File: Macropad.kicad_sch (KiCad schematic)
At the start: 19 parts, among them U1 Arduino_Pro_Micro

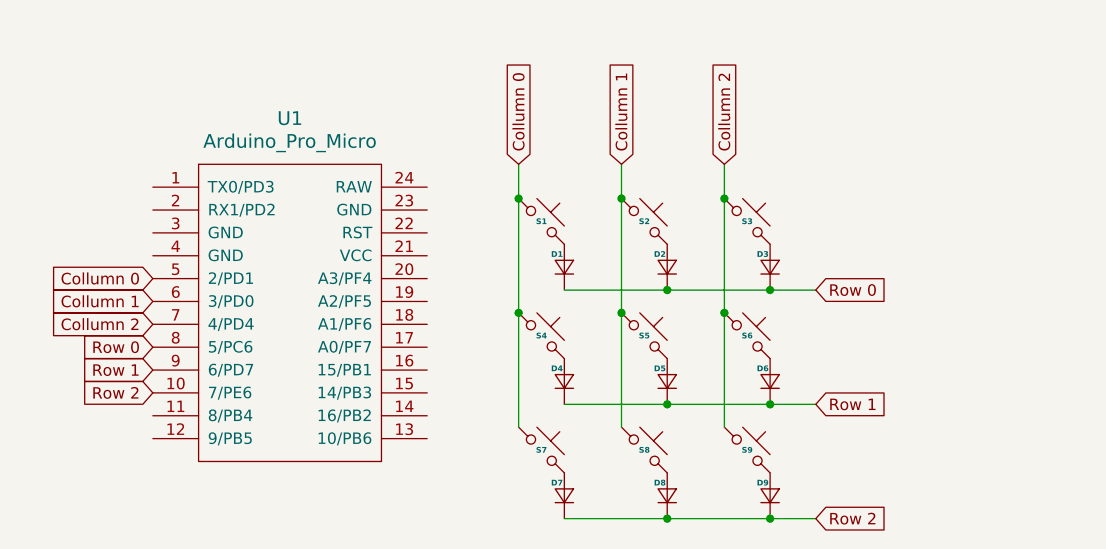
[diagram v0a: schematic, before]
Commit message: Change PCB dimension + add GND and Reset Button
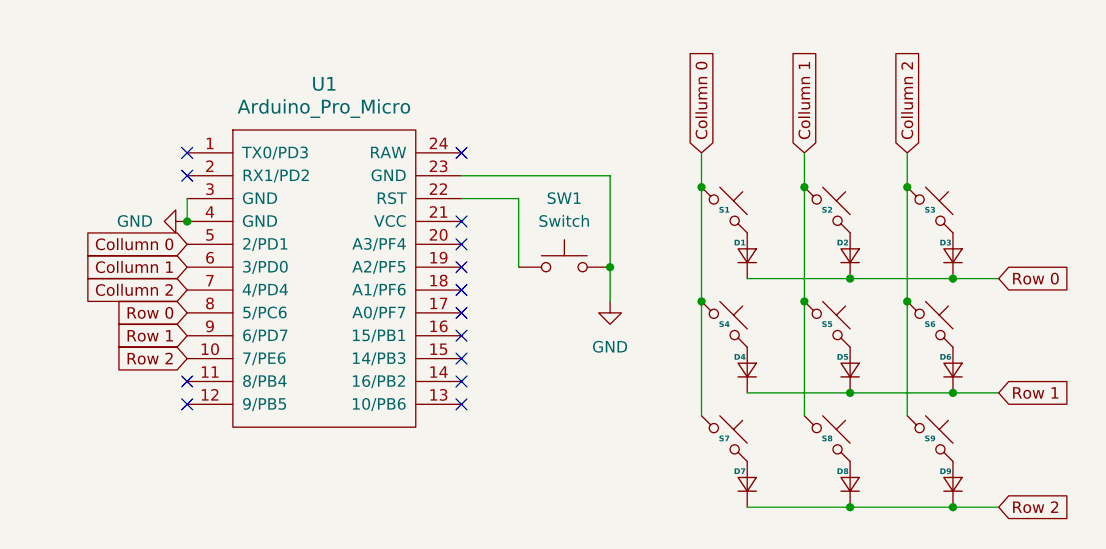
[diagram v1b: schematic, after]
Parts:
- added SW1: Switch, Button_Switch_THT:SW_PUSH_6mm, symbol ScottoKeebs:Placeholder_Switch
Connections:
- net at U1.22 (RST): now also SW1.1
- net GND: now reaches U1.23 (GND)
- net GND: now also U1.3 (GND), U1.4 (GND), SW1.2
- no-connect marks 0 -> 14
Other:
- moved on the sheet: D1, D2, D3, D4, D5, D6, D7, D8, D9, S1, S2, S3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
